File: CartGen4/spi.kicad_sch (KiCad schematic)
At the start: 11 parts, among them J1 MEM2080-00-128-00-A, U10 IS25WP080D-JNLE, U11 DS1391U-33+, Y1 FC-135R 32.7680KA-E5

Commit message: Forgot to close footprint assignment tool
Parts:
- BT1: footprint (none) -> Battery:Battery_CR1225
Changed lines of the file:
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@@
       (effects (font (size 1.27 1.27)) (justify left))
     )
-    (property "Footprint" "" (id 2) (at 184.15 93.726 90)
+    (property "Footprint" "Battery:Battery_CR1225" (id 2) (at 184.15 93.726 90)
       (effects (font (size 1.27 1.27)) hide)
     )

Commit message: Changed most R and C to 0402 size
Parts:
- C33, C34, C35: footprint Capacitor_SMD:C_0603_1608Metric_Pad1.08x0.95mm_HandSolder -> Capacitor_SMD:C_0402_1005Metric_Pad0.74x0.62mm_HandSolder
- R16, R17, R18: footprint Resistor_SMD:R_0603_1608Metric_Pad0.98x0.95mm_HandSolder -> Resistor_SMD:R_0402_1005Metric_Pad0.72x0.64mm_HandSolder
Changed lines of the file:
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@@
       (effects (font (size 1.27 1.27)) (justify left))
     )
-    (property "Footprint" "Resistor_SMD:R_0603_1608Metric_Pad0.98x0.95mm_HandSolder" (id 2) (at 165.862 69.85 90)
+    (property "Footprint" "Resistor_SMD:R_0402_1005Metric_Pad0.72x0.64mm_HandSolder" (id 2) (at 165.862 69.85 90)
       (effects (font (size 1.27 1.27)) hide)
     )
@@
       (effects (font (size 1.27 1.27)) (justify left))
     )
-    (property "Footprint" "Capacitor_SMD:C_0603_1608Metric_Pad1.08x0.95mm_HandSolder" (id 2) (at 119.0752 80.01 0)
+    (property "Footprint" "Capacitor_SMD:C_0402_1005Metric_Pad0.74x0.62mm_HandSolder" (id 2) (at 119.0752 80.01 0)
       (effects (font (size 1.27 1.27)) hide)
     )
@@
       (effects (font (size 1.27 1.27)) (justify left))
     )
-    (property "Footprint" "Capacitor_SMD:C_0603_1608Metric_Pad1.08x0.95mm_HandSolder" (id 2) (at 59.3852 135.89 0)
+    (property "Footprint" "Capacitor_SMD:C_0402_1005Metric_Pad0.74x0.62mm_HandSolder" (id 2) (at 59.3852 135.89 0)
       (effects (font (size 1.27 1.27)) hide)
     )
@@
       (effects (font (size 1.27 1.27)) (justify left))
     )
-    (property "Footprint" "Resistor_SMD:R_0603_1608Metric_Pad0.98x0.95mm_HandSolder" (id 2) (at 43.942 139.7 90)
+    (property "Footprint" "Resistor_SMD:R_0402_1005Metric_Pad0.72x0.64mm_HandSolder" (id 2) (at 43.942 139.7 90)
       (effects (font (size 1.27 1.27)) hide)
     )
@@
       (effects (font (size 1.27 1.27)) (justify left))
     )
-    (property "Footprint" "Capacitor_SMD:C_0603_1608Metric_Pad1.08x0.95mm_HandSolder" (id 2) (at 253.6952 78.74 0)
+    (property "Footprint" "Capacitor_SMD:C_0402_1005Metric_Pad0.74x0.62mm_HandSolder" (id 2) (at 253.6952 78.74 0)
       (effects (font (size 1.27 1.27)) hide)
     )
@@
       (effects (font (size 1.27 1.27)) (justify left))
     )
-    (property "Footprint" "Resistor_SMD:R_0603_1608Metric_Pad0.98x0.95mm_HandSolder" (id 2) (at 52.832 63.5 90)
-      (effects (font (size 1.27 1.27)) hide)
-    )
+    (property "Footprint" "Resistor_SMD:R_0402_1005Metric_Pad0.72x0.64mm_HandSolder" (id 2) (at 52.832 63.5 90)
+      (effects (font (size 1.27 1.27)) hide)
+    )

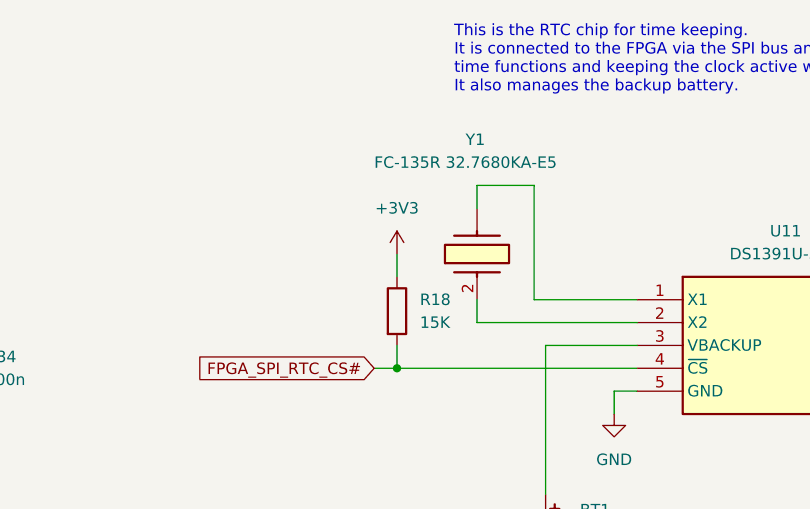
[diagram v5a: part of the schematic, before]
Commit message: Planned rough location of SPI peripherals
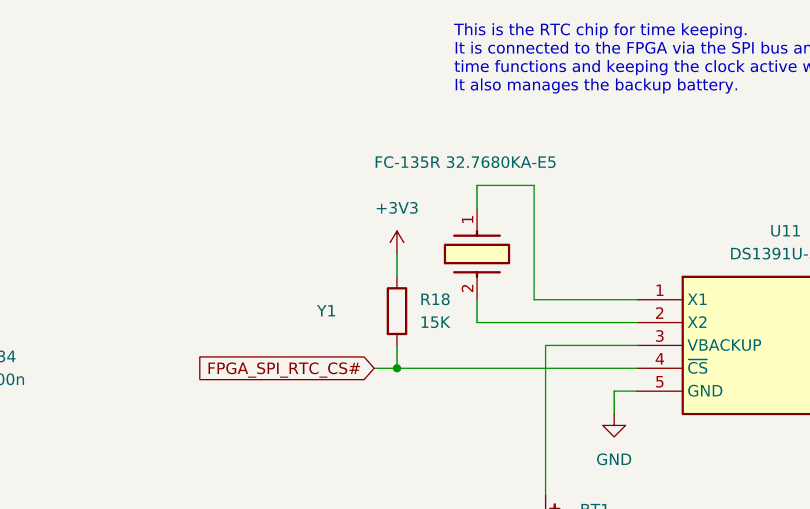
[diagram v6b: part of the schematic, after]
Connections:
- net at U11.1 (X1): now also Y1.1 (CRYSTAL_1); no longer Y1.
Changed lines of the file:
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@@
   (symbol (lib_id "SamacSys_Parts:FC-135R_32.7680KA-E5") (at 176.53 68.58 90) (unit 1)
     (in_bom yes) (on_board yes)
-    (property "Reference" "Y1" (id 0) (at 175.26 50.8 90)
+    (property "Reference" "Y1" (id 0) (at 158.75 69.85 90)
       (effects (font (size 1.27 1.27)) (justify right))
     )
@@
       (effects (font (size 1.27 1.27)) hide)
     )
-    (property "MFN" "Epson Timing" (id 11) (at 872.72 59.69 0)
+    (property "MFN" "Epson Timing" (id 11) (at 167.64 -627.61 0)
       (effects (font (size 1.27 1.27)) (justify left top) hide)
     )
-    (property "MFP" "FC-135R 32.7680KA-E3" (id 12) (at 972.72 59.69 0)
+    (property "MFP" "FC-135R 32.7680KA-E3" (id 12) (at 167.64 -727.61 0)
       (effects (font (size 1.27 1.27)) (justify left top) hide)
     )
@@
       (effects (font (size 1.27 1.27)) hide)
     )
-    (pin "")
+    (pin "1")
     (pin "2")
   )

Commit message: Chose battery retainer
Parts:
- BT1: footprint Battery:Battery_CR1225 -> SamacSys_Parts:2894
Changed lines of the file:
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@@
       (effects (font (size 1.27 1.27)) (justify left))
     )
-    (property "Footprint" "Battery:Battery_CR1225" (id 2) (at 184.15 93.726 90)
+    (property "Footprint" "SamacSys_Parts:2894" (id 2) (at 184.15 93.726 90)
       (effects (font (size 1.27 1.27)) hide)
     )
